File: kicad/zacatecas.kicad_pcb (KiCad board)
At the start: 2 copper layers, 99.1 x 97.8 mm, 53 parts, among them J1 LCD, J2 microSD, J3 CA1, J4 nanoLink, J5 STEP, J6 POWER, J7 SS22, Q1 BC548, Q2 BC548, Q3 BC548, SW1 RESET, SW10 7, SW2 NMI, SW3 3, SW4 1, SW5 0, SW6 2, SW7 4, SW8 6, SW9 5, U1 65C02, U2 65C22, U3 62256, U4 74HC132, U5 74HC32, U6 27C128, X1 1 MHz

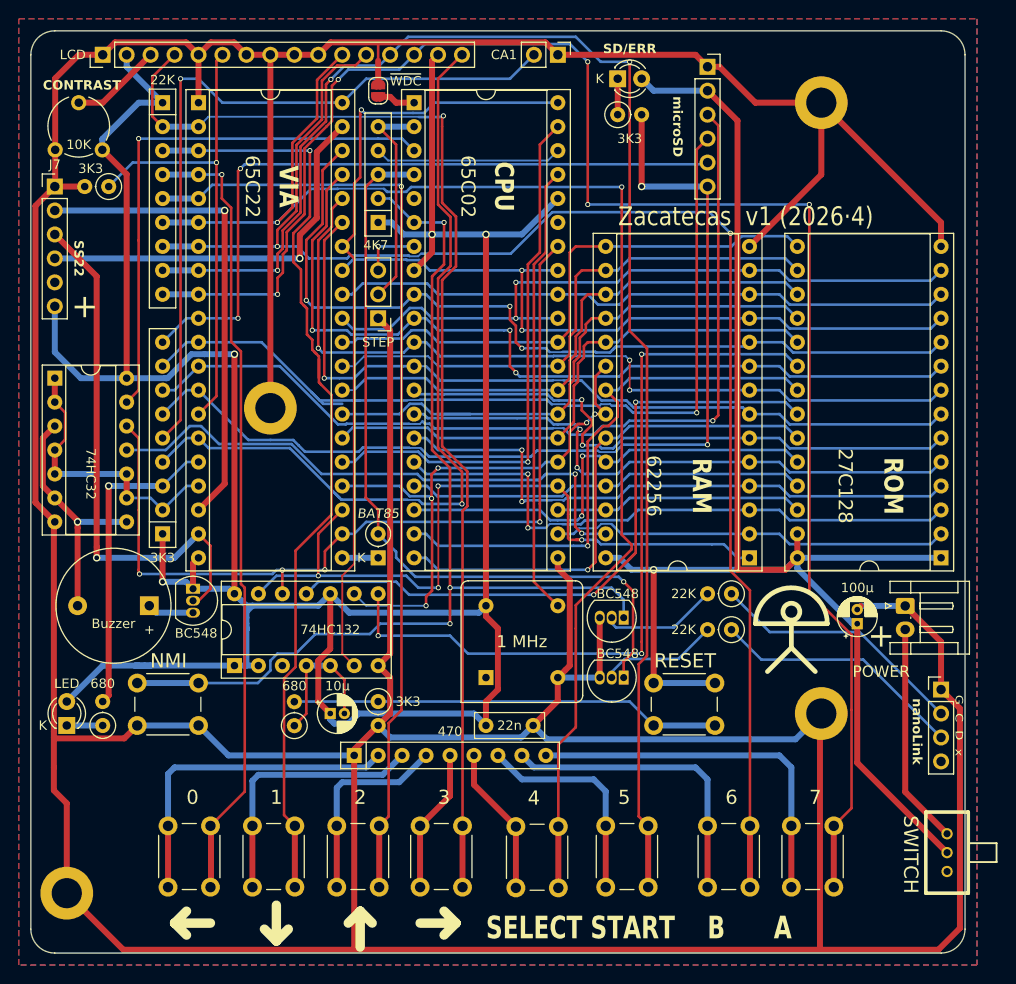
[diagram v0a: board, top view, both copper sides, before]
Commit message: fix LCD and add pad test
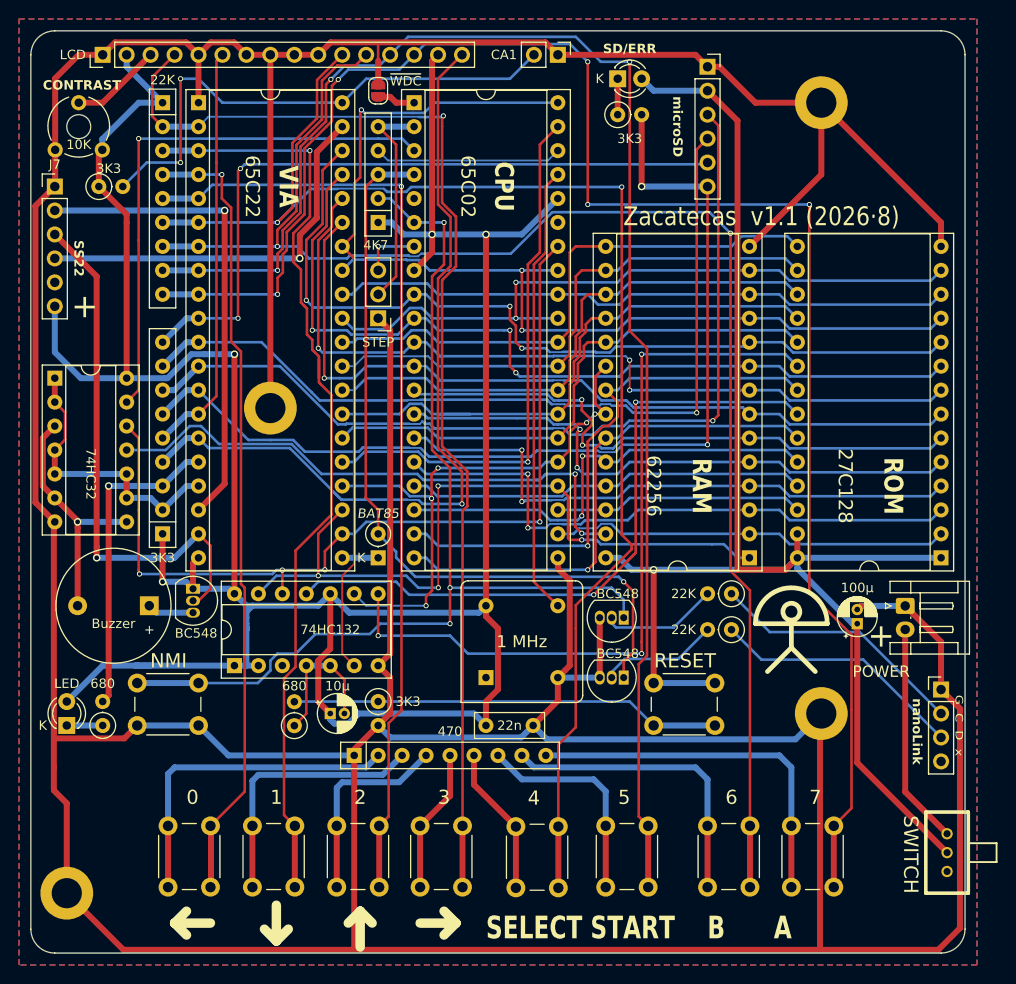
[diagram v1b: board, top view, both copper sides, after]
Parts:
- moved R6 1.05 mm to (35.1, 36.8), turned to 0 degrees
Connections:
- R6 pad 1: PB4 -> +5V
- R6 pad 2: GND -> /CA1
- RN3 pad 5: /CA1 -> PB4
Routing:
- net /CA1: track 79.5 -> 56.7 mm, vias 1 -> 2
- net PB4: track 51.6 -> 44.0 mm, vias 1 -> 0
- net PB1: track 94.9 -> 90.8 mm
- net GND: track 615.5 -> 612.4 mm
- net A14: track 78.7 -> 78.0 mm
- net /ROM_~{CS}: track 82.6 -> 82.0 mm
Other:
- outline, holes or cut-outs redrawn
- board text added: "Zacatecas v1.1 (2026·8)"
- board text removed: "Zacatecas v1 (2026·4)"
